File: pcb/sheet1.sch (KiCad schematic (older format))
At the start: 316 parts, among them J16 Aud_Conn, J17 Main_Connector, J18 Cat_Box_Conn, J20 J20, Q1 2N3904, Q3 Q_NPN_BCE, Q4 Q_NPN_BCE, SW3 E/F_10, SW4 D_10, Y1 12.096MHz

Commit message: Placed all the ICs
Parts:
- added unit 1 of K_8
- A_6, A_7, B_6, B_7, C_10, C_6, C_7, C_9, D_3, D_9, E_3, F_3, F_6, H_3, H_6, J_2, J_3, J_6, K_3, L/M_9, L_2, L_3, L_6, L_8, M_6, M_8, N_2, N_4, N_5, N_6, N_7, SW3: footprint (none) -> Star_Wars_Vector_PCB:DIP16
- A_8, A_9, B_5, B_9, C_5, C_8, D_5, D_8, E_5, E_6, E_7, E_8, F_7, F_8, H_8, J_5, K_2, K_5, K_6, K_8, L_10, M_2, M_3, N_8: footprint (none) -> Star_Wars_Vector_PCB:DIP14
- B_8, D_4, D_6, D_7, E/F_2, E_4, E_9, F_4, F_9, H_4, H_9, J_4, J_9, K_4, L_4, L_5, M_4, M_5, M_7, N_3: footprint (none) -> Star_Wars_Vector_PCB:DIP20
- C_2: footprint (none) -> Star_Wars_Vector_PCB:DDIP40
- F/H_2, F_5, H_5: footprint (none) -> Star_Wars_Vector_PCB:DDIP24
- H_7, J_7, K_7, L_7: footprint (none) -> Star_Wars_Vector_PCB:DIP18
- K_9: footprint (none) -> Star_Wars_Main_PCB:DIP28
- N_11: footprint (none) -> Star_Wars_Vector_PCB:DIP8
- SW1: renamed from L_11; value SW_DIP_x04 -> L_11; footprint (none) -> Star_Wars_Vector_PCB:DIP8
- SW2: renamed from SW4; footprint (none) -> Star_Wars_Vector_PCB:DIP16
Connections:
- net +5V: now also K_8.14 (VCC)
- net GND: now also K_8.7 (GND)
- no-connect marks 178 -> 180

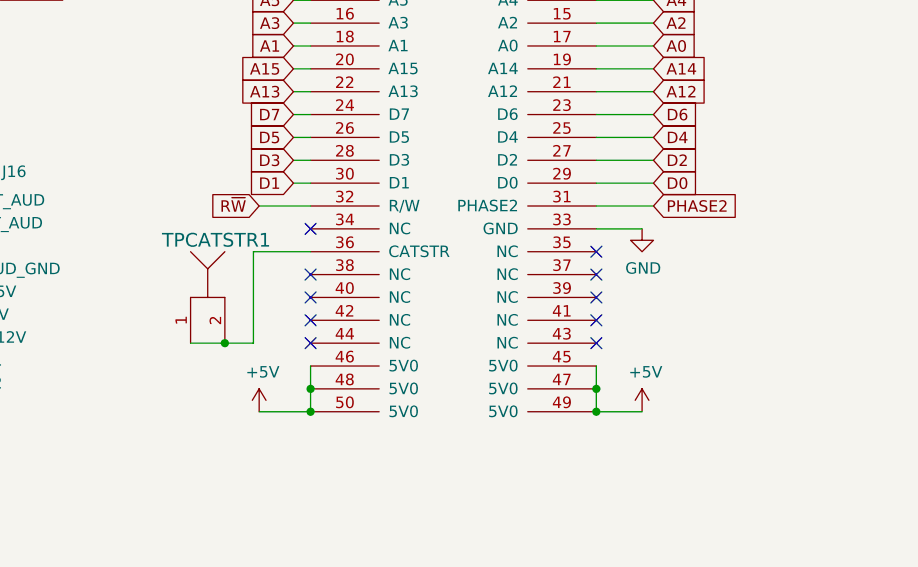
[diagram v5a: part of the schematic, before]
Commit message: Added power traces and components
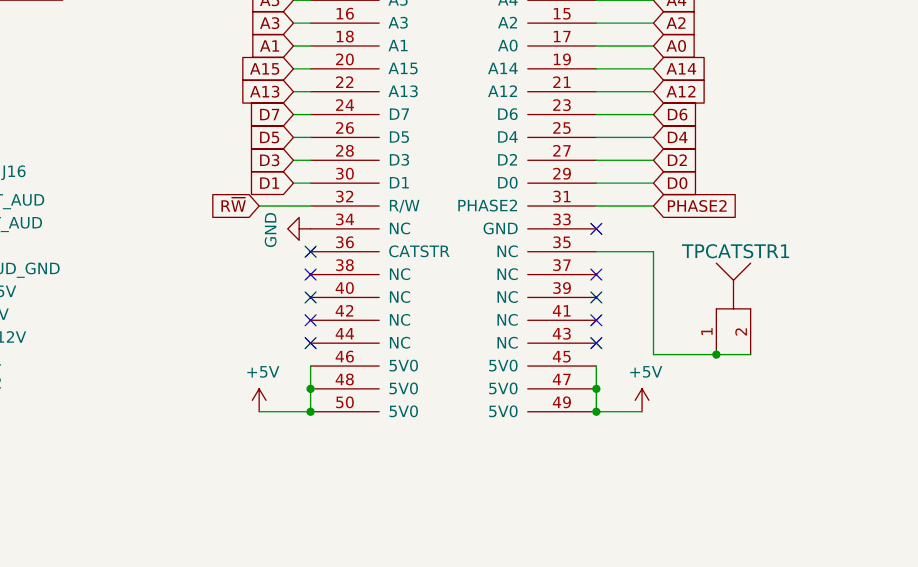
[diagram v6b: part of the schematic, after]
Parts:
- C10, C11, C12, C13, C14, C15, C16, C17, C18, C19, C20, C22, C46, C47, C48, C53, C54, C55, C87, C9, C91, C95, C96, CR3, R100, R20, R22, R23, R24, R25, R26, R27, R28, R29, R30, R31, R32, R33, R34, R35, R36, R37, R38, R39, R40, R41, R42, R43, R44, R45, R46, R47, R48, R49, R50, R51, R52, R53, R54, R55, R56, R57, R59, R79, R80, R81, R82, R83, R84, R85, R86: footprint (none) -> Star_Wars_Vector_PCB:GenericComp
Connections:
- net GND: now also J18.34 (NC); no longer J18.33 (GND)
- net at J18.35 (NC): now also TPCATSTR1.1, TPCATSTR1.2
- now unconnected: J18.36 (CATSTR)
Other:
- moved on the sheet: TPCATSTR1

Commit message: Added more power traces and components
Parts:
- TP+10.3UN1, TP+5V2, TPCOINL1, TPCOINR1, TPCOIN_AUX1, TPRST1, TPRST2, TPSELF_TEST1, TPSLAM1: footprint (none) -> Star_Wars_Vector_PCB:TEST_POINT
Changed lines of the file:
@@
 F 0 "TPRST2" H 7625 6150 60  0000 L CNN
 F 1 "TP" H 7700 5950 60  0001 C CNN
-F 2 "" H 7700 5850 60  0001 C CNN
+F 2 "Star_Wars_Vector_PCB:TEST_POINT" H 7700 5850 60  0001 C CNN
 F 3 "" H 7700 5850 60  0001 C CNN
 	1    7775 5900
@@
 F 0 "TPRST1" H 7275 6150 60  0000 L CNN
 F 1 "TP" H 7350 5950 60  0001 C CNN
-F 2 "" H 7350 5850 60  0001 C CNN
+F 2 "Star_Wars_Vector_PCB:TEST_POINT" H 7350 5850 60  0001 C CNN
 F 3 "" H 7350 5850 60  0001 C CNN
 	1    7425 5900
@@
 F 0 "TP+5V2" H 3669 2217 60  0000 L CNN
 F 1 "TP" H 3475 2275 60  0001 C CNN
-F 2 "" H 3475 2175 60  0001 C CNN
+F 2 "Star_Wars_Vector_PCB:TEST_POINT" H 3475 2175 60  0001 C CNN
 F 3 "" H 3475 2175 60  0001 C CNN
 	1    3550 2225
@@
 F 0 "TP+10.3UN1" H 1919 7117 60  0000 L CNN
 F 1 "TP" H 1725 7175 60  0001 C CNN
-F 2 "" H 1725 7075 60  0001 C CNN
+F 2 "Star_Wars_Vector_PCB:TEST_POINT" H 1725 7075 60  0001 C CNN
 F 3 "" H 1725 7075 60  0001 C CNN
 	1    1800 7125
@@
 F 0 "TPSLAM1" H 4850 12025 60  0000 L CNN
 F 1 "TP" H 4975 11825 60  0001 C CNN
-F 2 "" H 4975 11725 60  0001 C CNN
+F 2 "Star_Wars_Vector_PCB:TEST_POINT" H 4975 11725 60  0001 C CNN
 F 3 "" H 4975 11725 60  0001 C CNN
 	1    5050 11775
@@
 F 0 "TPSELF_TEST1" H 5175 12100 60  0000 L CNN
 F 1 "TP" H 5375 11825 60  0001 C CNN
-F 2 "" H 5375 11725 60  0001 C CNN
+F 2 "Star_Wars_Vector_PCB:TEST_POINT" H 5375 11725 60  0001 C CNN
 F 3 "" H 5375 11725 60  0001 C CNN
 	1    5450 11775
@@
 F 0 "TPCOINR1" H 4850 13850 60  0000 L CNN
 F 1 "TP" H 4975 13650 60  0001 C CNN
-F 2 "" H 4975 13550 60  0001 C CNN
+F 2 "Star_Wars_Vector_PCB:TEST_POINT" H 4975 13550 60  0001 C CNN
 F 3 "" H 4975 13550 60  0001 C CNN
 	1    5050 13600
@@
 F 0 "TPCOINL1" H 5350 13850 60  0000 L CNN
 F 1 "TP" H 5475 13650 60  0001 C CNN
-F 2 "" H 5475 13550 60  0001 C CNN
+F 2 "Star_Wars_Vector_PCB:TEST_POINT" H 5475 13550 60  0001 C CNN
 F 3 "" H 5475 13550 60  0001 C CNN
 	1    5550 13600
@@
 F 0 "TPCOIN_AUX1" H 5800 13850 60  0000 L CNN
 F 1 "TP" H 6025 13650 60  0001 C CNN
-F 2 "" H 6025 13550 60  0001 C CNN
+F 2 "Star_Wars_Vector_PCB:TEST_POINT" H 6025 13550 60  0001 C CNN
 F 3 "" H 6025 13550 60  0001 C CNN
 	1    6100 13600

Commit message: Added more components
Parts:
- C4, C7, C8, CR1, R12, R15, R18, R19, R21, R5, R6, R7, R8, R9: footprint (none) -> Star_Wars_Vector_PCB:GenericComp
- C49, C50, C51: footprint (none) -> Star_Wars_Vector_PCB:LargeCap
- Q3, Q4, VR1: footprint (none) -> Star_Wars_Vector_PCB:VoltReg
- TP+12V1, TP+5V1, TP-5V1, TPGND1, TPGND2: footprint (none) -> Star_Wars_Vector_PCB:TEST_POINT
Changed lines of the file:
@@
 F 0 "C50" H 1535 1304 50  0000 R CNN
 F 1 "100uf 35V" H 1535 1395 50  0000 R CNN
-F 2 "" H 1650 1350 50  0001 C CNN
+F 2 "Star_Wars_Vector_PCB:LargeCap" H 1650 1350 50  0001 C CNN
 F 3 "~" H 1650 1350 50  0001 C CNN
 	1    1650 1350
@@
 F 0 "C49" H 1640 2746 50  0000 L CNN
 F 1 "100uf 35V" H 1640 2655 50  0000 L CNN
-F 2 "" H 1525 2700 50  0001 C CNN
+F 2 "Star_Wars_Vector_PCB:LargeCap" H 1525 2700 50  0001 C CNN
 F 3 "~" H 1525 2700 50  0001 C CNN
 	1    1525 2700
@@
 F 0 "TPGND1" H 3069 2767 60  0000 L CNN
 F 1 "TP" H 2875 2825 60  0001 C CNN
-F 2 "" H 2875 2725 60  0001 C CNN
+F 2 "Star_Wars_Vector_PCB:TEST_POINT" H 2875 2725 60  0001 C CNN
 F 3 "" H 2875 2725 60  0001 C CNN
 	1    2950 2775
@@
 F 0 "TPGND2" H 3669 2767 60  0000 L CNN
 F 1 "TP" H 3475 2825 60  0001 C CNN
-F 2 "" H 3475 2725 60  0001 C CNN
+F 2 "Star_Wars_Vector_PCB:TEST_POINT" H 3475 2725 60  0001 C CNN
 F 3 "" H 3475 2725 60  0001 C CNN
 	1    3550 2775
@@
 F 0 "C51" H 2140 7996 50  0000 L CNN
 F 1 "100uf 35V" H 2140 7905 50  0000 L CNN
-F 2 "" H 2025 7950 50  0001 C CNN
+F 2 "Star_Wars_Vector_PCB:LargeCap" H 2025 7950 50  0001 C CNN
 F 3 "~" H 2025 7950 50  0001 C CNN
 	1    2025 7950
@@
 F 0 "R15" V 17520 3375 50  0000 C CNN
 F 1 "10k" V 17611 3375 50  0000 C CNN
-F 2 "" V 17765 3365 50  0001 C CNN
+F 2 "Star_Wars_Vector_PCB:GenericComp" V 17765 3365 50  0001 C CNN
 F 3 "~" H 17725 3375 50  0001 C CNN
 	1    17725 3375
@@
 F 0 "R9" H 8593 5521 50  0000 L CNN
 F 1 "1k" H 8593 5430 50  0000 L CNN
-F 2 "" V 8565 5465 50  0001 C CNN
+F 2 "Star_Wars_Vector_PCB:GenericComp" V 8565 5465 50  0001 C CNN
 F 3 "~" H 8525 5475 50  0001 C CNN
 	1    8525 5475
@@
 F 0 "CR1" V 8954 5529 50  0000 L CNN
 F 1 "1N914" V 9045 5529 50  0000 L CNN
-F 2 "" H 9000 5450 50  0001 C CNN
+F 2 "Star_Wars_Vector_PCB:GenericComp" H 9000 5450 50  0001 C CNN
 F 3 "~" H 9000 5450 50  0001 C CNN
 	1    9000 5450
@@
 F 0 "R7" V 8800 4825 50  0000 C CNN
 F 1 "220" V 8650 4825 50  0000 C CNN
-F 2 "" V 8765 4815 50  0001 C CNN
+F 2 "Star_Wars_Vector_PCB:GenericComp" V 8765 4815 50  0001 C CNN
 F 3 "~" H 8725 4825 50  0001 C CNN
 	1    8725 4825
@@
 F 0 "R6" V 8225 4825 50  0000 C CNN
 F 1 "100k" V 8075 4825 50  0000 C CNN
-F 2 "" V 8190 4815 50  0001 C CNN
+F 2 "Star_Wars_Vector_PCB:GenericComp" V 8190 4815 50  0001 C CNN
 F 3 "~" H 8150 4825 50  0001 C CNN
 	1    8150 4825
@@
 F 0 "R5" V 7500 4825 50  0000 C CNN
 F 1 "10k" V 7350 4825 50  0000 C CNN
-F 2 "" V 7465 4815 50  0001 C CNN
+F 2 "Star_Wars_Vector_PCB:GenericComp" V 7465 4815 50  0001 C CNN
 F 3 "~" H 7425 4825 50  0001 C CNN
 	1    7425 4825
@@
 F 0 "R8" V 7500 5150 50  0000 C CNN
 F 1 "15k" V 7350 5150 50  0000 C CNN
-F 2 "" V 7465 5140 50  0001 C CNN
+F 2 "Star_Wars_Vector_PCB:GenericComp" V 7465 5140 50  0001 C CNN
 F 3 "~" H 7425 5150 50  0001 C CNN
 	1    7425 5150
@@
 F 0 "C4" H 7165 5021 50  0000 L CNN
 F 1 ".1uf" H 7165 4930 50  0000 L CNN
-F 2 "" H 7088 4825 50  0001 C CNN
+F 2 "Star_Wars_Vector_PCB:GenericComp" H 7088 4825 50  0001 C CNN
 F 3 "~" H 7050 4975 50  0001 C CNN
 	1    7050 4975
@@
 F 0 "TP-5V1" H 1544 992 60  0000 L CNN
 F 1 "TP" H 1350 1050 60  0001 C CNN
-F 2 "" H 1350 950 60  0001 C CNN
+F 2 "Star_Wars_Vector_PCB:TEST_POINT" H 1350 950 60  0001 C CNN
 F 3 "" H 1350 950 60  0001 C CNN
 	1    1425 1000
@@
 F 0 "TP+5V1" H 3069 2217 60  0000 L CNN
 F 1 "TP" H 2875 2275 60  0001 C CNN
-F 2 "" H 2875 2175 60  0001 C CNN
+F 2 "Star_Wars_Vector_PCB:TEST_POINT" H 2875 2175 60  0001 C CNN
 F 3 "" H 2875 2175 60  0001 C CNN
 	1    2950 2225
@@
 F 0 "VR1" H 3025 8042 50  0000 C CNN
 F 1 "L7805" H 3025 7951 50  0000 C CNN
-F 2 "" H 3050 7650 50  0001 L CIN
+F 2 "Star_Wars_Vector_PCB:VoltReg" H 3050 7650 50  0001 L CIN
 F 3 "http://www.st.com/content/ccc/resource/technical/document/datasheet/41/4f/b3/b0/12/d4/47/88/CD00000444.pdf/files/CD00000444.pdf/jcr:content/translations/en.CD00000444.pdf" H 3025 7750 50  0001 C CNN
 	1    3025 7800
@@
 F 0 "TP+12V1" H 1919 7592 60  0000 L CNN
 F 1 "TP" H 1725 7650 60  0001 C CNN
-F 2 "" H 1725 7550 60  0001 C CNN
+F 2 "Star_Wars_Vector_PCB:TEST_POINT" H 1725 7550 60  0001 C CNN
 F 3 "" H 1725 7550 60  0001 C CNN
 	1    1800 7600
@@
 F 0 "R12" V 27825 5375 50  0000 C CNN
 F 1 "10k" V 27975 5375 50  0000 C CNN
-F 2 "" V 27940 5365 50  0001 C CNN
+F 2 "Star_Wars_Vector_PCB:GenericComp" V 27940 5365 50  0001 C CNN
 F 3 "~" H 27900 5375 50  0001 C CNN
 	1    27900 5375
@@
 F 0 "Q3" H 38491 7246 50  0000 L CNN
 F 1 "Q_NPN_BCE" H 38491 7155 50  0000 L CNN
-F 2 "" H 38500 7300 50  0001 C CNN
+F 2 "Star_Wars_Vector_PCB:VoltReg" H 38500 7300 50  0001 C CNN
 F 3 "~" H 38300 7200 50  0001 C CNN
 	1    38300 7200
@@
 F 0 "Q4" H 38491 8071 50  0000 L CNN
 F 1 "Q_NPN_BCE" H 38491 7980 50  0000 L CNN
-F 2 "" H 38500 8125 50  0001 C CNN
+F 2 "Star_Wars_Vector_PCB:VoltReg" H 38500 8125 50  0001 C CNN
 F 3 "~" H 38300 8025 50  0001 C CNN
 	1    38300 8025
@@
 F 0 "C7" H 39190 7246 50  0000 L CNN
 F 1 ".1uf" H 39190 7155 50  0000 L CNN
-F 2 "" H 39113 7050 50  0001 C CNN
+F 2 "Star_Wars_Vector_PCB:GenericComp" H 39113 7050 50  0001 C CNN
 F 3 "~" H 39075 7200 50  0001 C CNN
 	1    39075 7200
@@
 F 0 "C8" H 39190 8071 50  0000 L CNN
 F 1 ".1uf" H 39190 7980 50  0000 L CNN
-F 2 "" H 39113 7875 50  0001 C CNN
+F 2 "Star_Wars_Vector_PCB:GenericComp" H 39113 7875 50  0001 C CNN
 F 3 "~" H 39075 8025 50  0001 C CNN
 	1    39075 8025
@@
 F 0 "R18" H 1793 9496 50  0000 L CNN
 F 1 "470" H 1793 9405 50  0000 L CNN
-F 2 "" V 1765 9440 50  0001 C CNN
+F 2 "Star_Wars_Vector_PCB:GenericComp" V 1765 9440 50  0001 C CNN
 F 3 "~" H 1725 9450 50  0001 C CNN
 	1    1725 9450
@@
 F 0 "R19" H 2068 9496 50  0000 L CNN
 F 1 "470" H 2068 9405 50  0000 L CNN
-F 2 "" V 2040 9440 50  0001 C CNN
+F 2 "Star_Wars_Vector_PCB:GenericComp" V 2040 9440 50  0001 C CNN
 F 3 "~" H 2000 9450 50  0001 C CNN
 	1    2000 9450
@@
 F 0 "R21" H 2618 9496 50  0000 L CNN
 F 1 "470" H 2618 9405 50  0000 L CNN
-F 2 "" V 2590 9440 50  0001 C CNN
+F 2 "Star_Wars_Vector_PCB:GenericComp" V 2590 9440 50  0001 C CNN
 F 3 "~" H 2550 9450 50  0001 C CNN
 	1    2550 9450
